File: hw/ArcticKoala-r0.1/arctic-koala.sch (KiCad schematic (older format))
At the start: 86 parts, among them J1 Jumper, J14 PMOD, J18 Jumper, J2 Jumper, J20 Flash, J21 PMOD, J22 PMOD, J23 PMOD, J26 5V AUX, J27 5V AUX, J29 Jumper, P1 pkl_USB_OTG, P2 UP, P3 UP, P4 UP, P5 UP, SW1 TACT, U1 93C46B-SOT-23-6, U2 PSRAM, U4 FT2232H, U5 W25Q128JV-DTR, U6 LIFCL40-NX, U7 12MHz

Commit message: Updated KiCad files
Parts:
- removed J14: PMOD, Connector_PinSocket_2.54mm:PinSocket_2x06_P2.54mm_Vertical, symbol Connector_Generic:Conn_02x06_Top_Bottom
- added J3: Conn_02x07_Odd_Even, Connector_PinSocket_2.54mm:PinSocket_2x07_P2.54mm_Vertical, symbol Connector_Generic:Conn_02x07_Odd_Even
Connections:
- net +3V3: now also J3.13 (Pin_13), J3.14 (Pin_14)
- net CK_N: now also J3.2 (Pin_2)
- net CK_P: now also J3.1 (Pin_1)
- net D0N: now also J3.4 (Pin_4)
- net D0P: now also J3.3 (Pin_3)
- net D1N: now also J3.6 (Pin_6)
- net D1P: now also J3.5 (Pin_5)
- net D2N: now also J3.8 (Pin_8)
- net D2P: now also J3.7 (Pin_7)
- net D3N: now also J3.10 (Pin_10)
- net D3P: now also J3.9 (Pin_9)
- net GND: now also J3.11 (Pin_11), J3.12 (Pin_12)
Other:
- note added: "TODO:\n\nVregs (3v3, 1v8, 1v0)\nCLK\nPSRAM_CS\nLEDs/Buttons\n"
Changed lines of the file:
@@
 EESchema Schematic File Version 4
-LIBS:icebreaker-cache
+LIBS:arctic-koala-cache
 EELAYER 30 0
 EELAYER END
@@
 	1    0    0    -1
 $EndComp
-$Comp
-L Connector_Generic:Conn_02x06_Top_Bottom J14
-U 1 1 5E0DEE98
-P 13250 1000
-F 0 "J14" H 13300 1400 50  0000 C CNN
-F 1 "PMOD" H 13300 1300 50  0000 C CNN
-F 2 "Connector_PinSocket_2.54mm:PinSocket_2x06_P2.54mm_Vertical" H 13250 1000 50  0001 C CNN
-F 3 "~" H 13250 1000 50  0001 C CNN
-F 4 "conn-th-01in-6-2-rec-ra" H 850 -1400 50  0001 C CNN "Key"
-F 5 "ANY" H 13250 1000 50  0001 C CNN "Source"
-	1    13250 1000
-	1    0    0    -1
-$EndComp
-Text Label 12750 800  2    50   ~ 0
+Text Label 12950 750  2    50   ~ 0
 CK_P
-Text Label 12750 900  2    50   ~ 0
+Text Label 13650 750  0    50   ~ 0
 CK_N
 Wire Wire Line
-	13050 800  12750 800
+	13050 750  12950 750
 Wire Wire Line
-	13050 900  12750 900
-Text Label 12750 1100 2    50   ~ 0
+	13550 750  13650 750
+Text Label 12950 850  2    50   ~ 0
 D0P
-Text Label 12750 1000 2    50   ~ 0
+Text Label 13650 850  0    50   ~ 0
 D0N
 Wire Wire Line
-	13050 1000 12750 1000
+	13550 850  13650 850
 Wire Wire Line
-	13050 1100 12750 1100
-Text Label 12750 1200 2    50   ~ 0
+	13050 850  12950 850
+Text Label 12950 950  2    50   ~ 0
 D1P
-Text Label 12750 1300 2    50   ~ 0
+Text Label 13650 950  0    50   ~ 0
 D1N
 Wire Wire Line
-	13050 1200 12750 1200
+	13050 950  12950 950
 Wire Wire Line
-	13050 1300 12750 1300
-Text Label 13850 900  0    50   ~ 0
+	13550 950  13650 950
+Text Label 13650 1050 0    50   ~ 0
 D2N
-Text Label 13850 800  0    50   ~ 0
+Text Label 12950 1050 2    50   ~ 0
 D2P
 Wire Wire Line
-	13550 900  13850 900
+	13550 1050 13650 1050
 Wire Wire Line
-	13550 800  13850 800
-Text Label 13850 1100 0    50   ~ 0
+	13050 1050 12950 1050
+Text Label 13650 1150 0    50   ~ 0
 D3N
-Text Label 13850 1000 0    50   ~ 0
+Text Label 12950 1150 2    50   ~ 0
 D3P
 Wire Wire Line
-	13550 1100 13850 1100
+	13550 1150 13650 1150
 Wire Wire Line
-	13550 1000 13850 1000
+	13050 1150 12950 1150
 $Comp
 L power:+3V3 #PWR0112
 U 1 1 5E277F12
-P 14200 1050
-F 0 "#PWR0112" H 14200 900 50  0001 C CNN
-F 1 "+3V3" H 14215 1226 50  0000 C CNN
-F 2 "" H 14200 1050 50  0001 C CNN
-F 3 "" H 14200 1050 50  0001 C CNN
-	1    14200 1050
+P 13950 1200
+F 0 "#PWR0112" H 13950 1050 50  0001 C CNN
+F 1 "+3V3" H 13965 1376 50  0000 C CNN
+F 2 "" H 13950 1200 50  0001 C CNN
+F 3 "" H 13950 1200 50  0001 C CNN
+	1    13950 1200
 	1    0    0    -1
 $EndComp
 Wire Wire Line
-	14200 1050 14200 1200
+	13950 1200 13950 1350
 Wire Wire Line
-	14200 1200 13550 1200
+	13950 1350 13550 1350
 Wire Wire Line
-	13550 1300 13650 1300
+	13550 1250 13650 1250
 Wire Wire Line
-	13650 1300 13650 1350
+	13650 1250 13650 1400
 $Comp
 L power:GND #PWR0113
 U 1 1 5E31EBCD
-P 13650 1350
-F 0 "#PWR0113" H 13650 1100 50  0001 C CNN
-F 1 "GND" H 13800 1300 50  0000 C CNN
-F 2 "" H 13650 1350 50  0001 C CNN
-F 3 "" H 13650 1350 50  0001 C CNN
-	1    13650 1350
+P 13650 1400
+F 0 "#PWR0113" H 13650 1150 50  0001 C CNN
+F 1 "GND" H 13800 1350 50  0000 C CNN
+F 2 "" H 13650 1400 50  0001 C CNN
+F 3 "" H 13650 1400 50  0001 C CNN
+	1    13650 1400
 	1    0    0    -1
 $EndComp
@@
 Wire Wire Line
 	8950 950  8950 850
-Text Notes 11800 1050 0    50   ~ 0
+Text Notes 11200 1000 0    50   ~ 0
 Note: D0 is inverted
 Text Label 5000 3650 0    50   ~ 0
@@
 Wire Wire Line
 	8500 9600 9300 9600
+Text Notes 2350 8850 0    50   ~ 0
+TODO:\n\nVregs (3v3, 1v8, 1v0)\nCLK\nPSRAM_CS\nLEDs/Buttons\n
+$Comp
+L Connector_Generic:Conn_02x07_Odd_Even J3
+U 1 1 5E073ED3
+P 13250 1050
+F 0 "J3" H 13300 1567 50  0000 C CNN
+F 1 "Conn_02x07_Odd_Even" H 13300 1476 50  0000 C CNN
+F 2 "Connector_PinSocket_2.54mm:PinSocket_2x07_P2.54mm_Vertical" H 13250 1050 50  0001 C CNN
+F 3 "~" H 13250 1050 50  0001 C CNN
+	1    13250 1050
+	1    0    0    -1
+$EndComp
+$Comp
+L power:+3V3 #PWR0157
+U 1 1 5E385C4C
+P 12650 1200
+F 0 "#PWR0157" H 12650 1050 50  0001 C CNN
+F 1 "+3V3" H 12665 1376 50  0000 C CNN
+F 2 "" H 12650 1200 50  0001 C CNN
+F 3 "" H 12650 1200 50  0001 C CNN
+	1    12650 1200
+	-1   0    0    -1
+$EndComp
+Wire Wire Line
+	12650 1200 12650 1350
+Wire Wire Line
+	12650 1350 13050 1350
+Wire Wire Line
+	13050 1250 12950 1250
+Wire Wire Line
+	12950 1250 12950 1400
+$Comp
+L power:GND #PWR0158
+U 1 1 5E385C5A
+P 12950 1400
+F 0 "#PWR0158" H 12950 1150 50  0001 C CNN
+F 1 "GND" H 13100 1350 50  0000 C CNN
+F 2 "" H 12950 1400 50  0001 C CNN
+F 3 "" H 12950 1400 50  0001 C CNN
+	1    12950 1400
+	-1   0    0    -1
+$EndComp
 $EndSCHEMATC

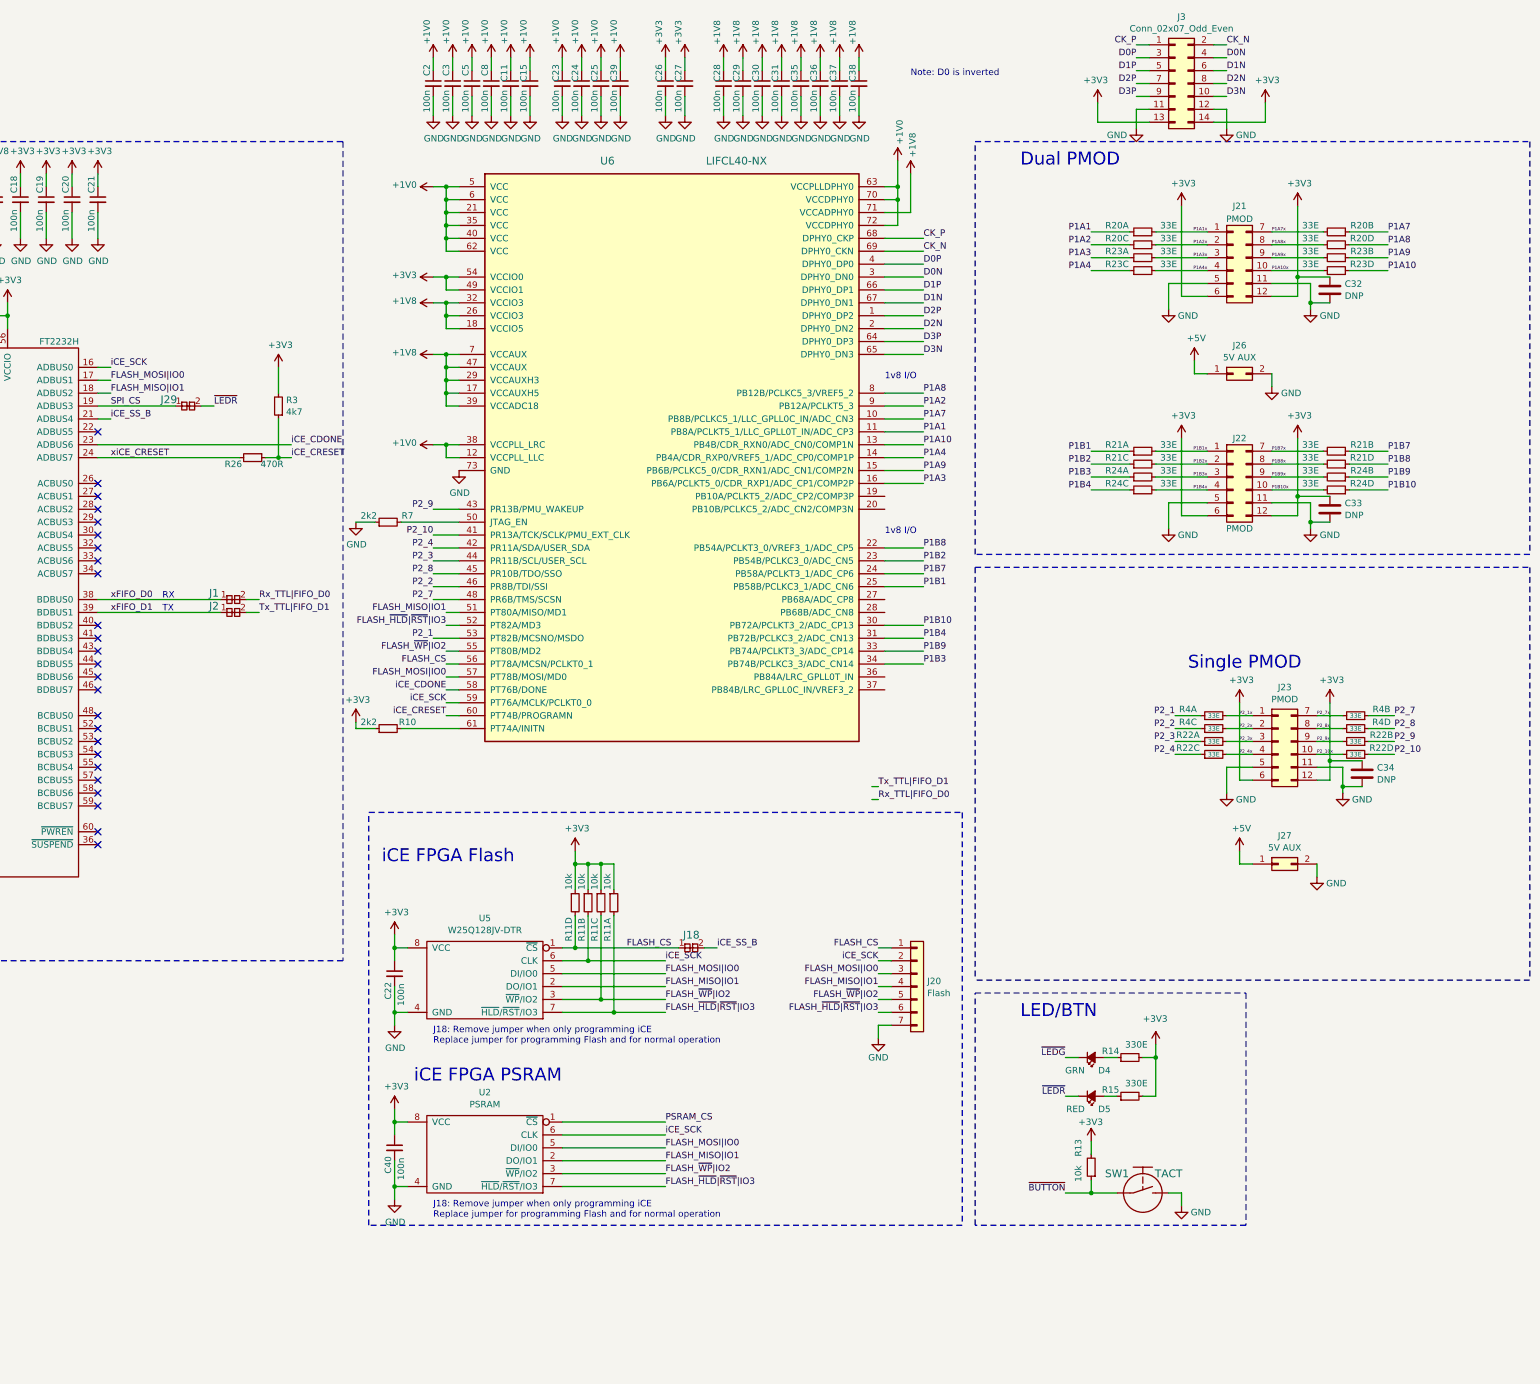
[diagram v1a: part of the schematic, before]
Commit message: Added ESD protection to MIPI lines
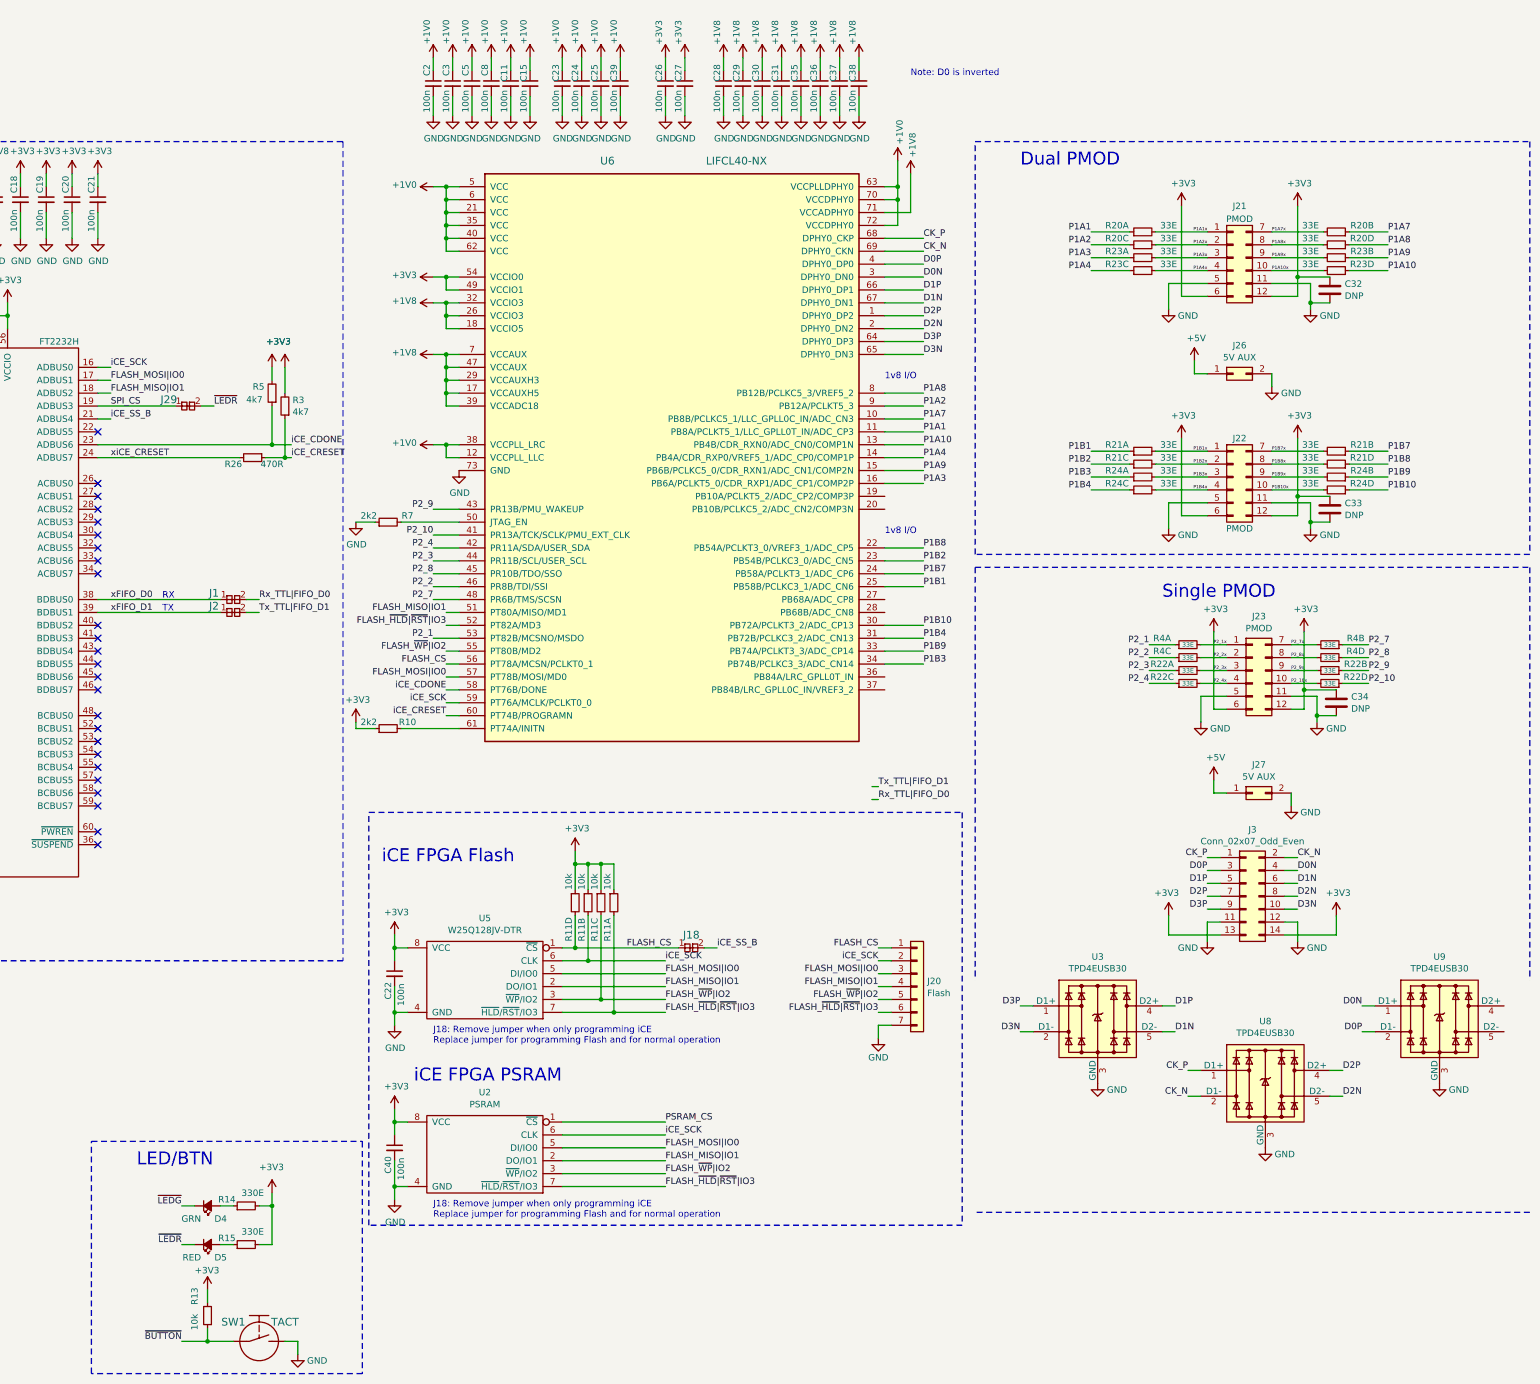
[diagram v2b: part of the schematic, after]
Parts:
- added R5: 4k7, pkl_dipol:R_0402, symbol pkl_device:pkl_R_Small
- added U3, U8, U9: TPD4EUSB30, Package_SON:USON-10_2.5x1.0mm_P0.5mm, symbol Power_Protection:TPD4EUSB30
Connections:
- net +3V3: now also R5.2
- net CK_N: now also U8.2 (D1-)
- net CK_P: now also U8.1 (D1+)
- net D0N: now also U9.1 (D1+)
- net D0P: now also U9.2 (D1-)
- net D1N: now also U3.5 (D2-)
- net D1P: now also U3.4 (D2+)
- net D2N: now also U8.5 (D2-)
- net D2P: now also U8.4 (D2+)
- net D3N: now also U3.2 (D1-)
- net D3P: now also U3.1 (D1+)
- net GND: now also U3.3 (GND), U3.8 (GND), U8.3 (GND), U8.8 (GND), U9.3 (GND), U9.8 (GND)
- net iCE_CDONE: now also R5.1
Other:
- moved on the sheet: C34, D4, D5, J23, J27, J3, R13, R14, R15, R22A, R22B, R22C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

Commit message: Completed hardware design files
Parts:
- removed C10: 100n, pkl_dipol:C_0402, symbol pkl_device:pkl_C_Small
- removed C7: 4u7, pkl_dipol:C_0603, symbol pkl_device:pkl_C
- removed D4: GRN, pkl_dipol:D_0603, symbol pkl_device:pkl_Led_Small
- added C10, C42, C46, C48, C49, C50: 4.7uF, pkl_dipol:C_0402, symbol Device:C
- added C41, C45, C7: 22pF, pkl_dipol:C_0402, symbol Device:C
- added C43: 4.7uF, pkl_dipol:C_0603, symbol Device:C
- added C44, C47: 100nF, pkl_dipol:C_0402, symbol Device:C
- added L3, L4, L5: 1.0uH, Inductor_SMD:L_0603_1608Metric, symbol Device:L_Small
- added R12, R16, R17, R18, R19, R25: R, pkl_dipol:R_0402, symbol Device:R
- added R27, R28: 2k2, pkl_dipol:R_0402, symbol pkl_device:pkl_R_Small
- added R29: 4k7, pkl_dipol:R_0402, symbol pkl_device:pkl_R_Small
- added U10, U11, U12: TPS62067, Package_SON:WSON-8-1EP_2x2mm_P0.5mm_EP0.9x1.6mm_ThermalVias, symbol gkl_pmic:TPS62067
- R14: value 330E -> 30R; Key res-0402-330 -> res-0402-2k2
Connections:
- net +1V0: now also C10.1, C48.1, C7.1, L4.2, R17.1
- net +1V8: now also R13.2, C45.1, C46.1, C49.1, L5.2, R19.1; no longer U4.49 (VREGOUT)
- net +3V3: now also C41.1, C42.1, C44.1, C47.1, C50.1, L3.2, R12.1, R29.2, U11.5 (EN), U11.7 (AVIN), U11.8 (PVIN), U12.5 (EN), U12.7 (AVIN), U12.8 (PVIN); no longer R13.2, R14.2, U4.50 (VREGIN)
- net +5V: now also C43.1, U10.5 (EN), U10.7 (AVIN), U10.8 (PVIN)
- net FTDI_CLK: now also R14.2
- net GND: now also C10.2, C42.2, C43.2, C44.2, C46.2, C47.2, C48.2, C49.2, C50.2, R16.2, R18.2, R25.2, R28.2, U10.1 (PGND), U10.3 (AGND), U10.9 (GND), U11.1 (PGND), U11.3 (AGND), U11.9 (GND), U12.1 (PGND), U12.3 (AGND), U12.9 (GND)
- net PSRAM_CS: now also U6.20 (PB10B/PCLKC5_2/ADC_CN2/COMP3N), R29.1
- net Rx_TTL|FIFO_D0: now also R27.1
- net Tx_TTL|FIFO_D1: now also U6.36 (PB84A/LRC_GPLL0T_IN)
- net ~BUTTON: now also U6.27 (PB68A/ADC_CP8)
- net ~LEDR: now also U6.28 (PB68B/ADC_CN8)
- net at R14.1: now also U6.19 (PB10A/PCLKT5_2/ADC_CP2/COMP3P)
- net at U6.37 (PB84B/LRC_GPLL0C_IN/VREF3_2): now also R27.2, R28.1
- new net: L3.1, U10.2 (SW)
- new net: C41.2, R12.2, R16.1, U10.4 (FB)
- new net: L5.1, U12.2 (SW)
- new net: C45.2, R19.2, R25.1, U12.4 (FB)
- new net: L4.1, U11.2 (SW)
- new net: C7.2, R17.2, R18.1, U11.4 (FB)
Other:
- note added: "\n"
- note removed: "TODO:\n\nVregs (3v3, 1v8, 1v0)\nCLK\nPSRAM_CS\nLEDs/Buttons\n"
- moved on the sheet: D5, R13, R15, SW1

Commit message: hw: Add Gerbers, BOM
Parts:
- added D1: BLUE, pkl_dipol:D_0603, symbol pkl_device:pkl_Led_Small
- added D2: GREEN, pkl_dipol:D_0603, symbol pkl_device:pkl_Led_Small
- added R30: 330E, pkl_dipol:R_0402, symbol pkl_device:pkl_R_Small
- C1, C11, C12, C13, C14, C15, C16, C17, C18, C19, C2, C20, C21, C22, C23, C24, C25, C26, C27, C28, C29, C3, C30, C31, C35, C36, C37, C38, C39, C4, C40, C5, C8: Mfg (none) -> Samsung Electro-Mechanics; PN (none) -> CL05B104KO5NNNC
- C10, C42, C46, C48, C49, C50: Mfg (none) -> Samsung Electro-Mechanics; PN (none) -> CL05A475MP5NRNC
- C32, C33, C34: value DNP -> 10uF; Mfg (none) -> Samsung Electro-Mechanics; PN (none) -> CL10A106KP8NNNC
- C41, C45, C7: Mfg (none) -> Samsung Electro-Mechanics; PN (none) -> CL05C220JB5NNNC
- C43: value 4.7uF -> 10uF; Mfg (none) -> Samsung Electro-Mechanics; PN (none) -> CL10A106KP8NNNC
- C44, C47: value 100nF -> 100n; Mfg (none) -> Samsung Electro-Mechanics; PN (none) -> CL05B104KO5NNNC
- C6, C9: Mfg (none) -> Samsung Electro-Mechanics; PN (none) -> CL10A475KP8NNNC
- D5: Mfg (none) -> Wurth Electronics Inc. (VA); PN (none) -> 150060SS75000
- J21, J22: Mfg (none) -> Sullins Connector Solutions; PN (none) -> PPPC062LJBN-RC
- J23: footprint Socket_Strips:Socket_Strip_Straight_2x06 -> Socket_Strips:Socket_Strip_Angled_2x06; Mfg (none) -> Sullins Connector Solutions; PN (none) -> PPPC062LJBN-RC
- J3: Mfg (none) -> Sullins Connector Solutions; PN (none) -> PPPC072LJBN-RC
- L1, L2: Mfg (none) -> Murata Electronics North America; PN (none) -> BLM15AG601SN1D
- L3, L4, L5: Mfg (none) -> Littelfuse Inc.; PN (none) -> LPWI160808S1R0T
- P1: Mfg (none) -> Amphenol FCI (VA); PN (none) -> 10118192-0001LF
- R1: Mfg (none) -> PANASONIC ELECTRONIC COMPONENTS (VA); PN (none) -> ERJ-2RKF1004X
- R10, R27, R28, R6, R7: Mfg (none) -> PANASONIC ELECTRONIC COMPONENTS (VA); PN (none) -> ERJ-2RKF2201X
- R11, R2: Mfg (none) -> PANASONIC ELECTRONIC COMPONENTS (VA); PN (none) -> EXB-28V103JX
- R12: value R -> 450k; Mfg (none) -> PANASONIC ELECTRONIC COMPONENTS (VA); PN (none) -> ERJ-2RKF4533X
- R13, R9: Mfg (none) -> PANASONIC ELECTRONIC COMPONENTS (VA); PN (none) -> ERJ-2RKF1002X
- R14: Mfg (none) -> PANASONIC ELECTRONIC COMPONENTS (VA); PN (none) -> ERJ-2RKF30R0X
- R15: Mfg (none) -> PANASONIC ELECTRONIC COMPONENTS (VA); PN (none) -> ERJ-2RKF3300X
- R16: value R -> 100k; Mfg (none) -> PANASONIC ELECTRONIC COMPONENTS (VA); PN (none) -> ERJ-2RKF1003X
- R17: value R -> 120k; Mfg (none) -> PANASONIC ELECTRONIC COMPONENTS (VA); PN (none) -> ERJ-2RKF1203X
- R18, R25: value R -> 180k; Mfg (none) -> PANASONIC ELECTRONIC COMPONENTS (VA); PN (none) -> ERJ-2RKF1803X
- R19: value R -> 360k; Mfg (none) -> PANASONIC ELECTRONIC COMPONENTS (VA); PN (none) -> ERJ-2RKF3603X
- R20, R21, R22, R23, R24, R4: Mfg (none) -> PANASONIC ELECTRONIC COMPONENTS (VA); PN (none) -> EXB-28V330JX
- R26: Mfg (none) -> PANASONIC ELECTRONIC COMPONENTS (VA); PN (none) -> ERJ-2RKF4700X
- R29, R3: Mfg (none) -> PANASONIC ELECTRONIC COMPONENTS (VA); PN (none) -> ERJ-2RKF4701X
- R5: value 4k7 -> 2k2; Mfg (none) -> PANASONIC ELECTRONIC COMPONENTS (VA); PN (none) -> ERJ-2RKF2201X
- R8: Mfg (none) -> Yageo; PN (none) -> RC0402FR-0712KL
- SW1: Mfg (none) -> C&K (VA); PN (none) -> KMR621NG LFS
- U1: Mfg (none) -> Microchip Technology (VA); PN (none) -> 93C46BT-I/OT
- U10, U11, U12: Mfg (none) -> Texas Instruments; PN (none) -> TPS62067DSGR
- U2: Mfg (none) -> Lyontek Inc.; PN (none) -> LY68L6400SLIT
- U3, U8, U9: Mfg (none) -> Texas Instruments; PN (none) -> TPD4E05U06DQAR
- U4: Mfg (none) -> FTDI, Future Technology Devices International Ltd (VA); PN (none) -> FT2232HQ-REEL
- U5: Mfg (none) -> Winbond Electronics (VA); PN (none) -> W25Q128JVSIM TR
- U6: Mfg (none) -> Lattice Semiconductor Corporation; PN (none) -> LIFCL-40-8SG72CES
- U7: Mfg (none) -> SiTIME (VA); PN (none) -> SIT2001BI-S2-33E-12.000000G
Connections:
- net +3V3: now also R30.2
- net GND: now also D1.C, D2.C
- net iCE_CDONE: now also D1.A
- new net: D2.A, R30.1
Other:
- moved on the sheet: R13, R5, SW1
